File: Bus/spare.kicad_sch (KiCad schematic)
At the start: 2 parts, among them J16 Conn_01x06_Pin, J17 Conn_01x03_Pin

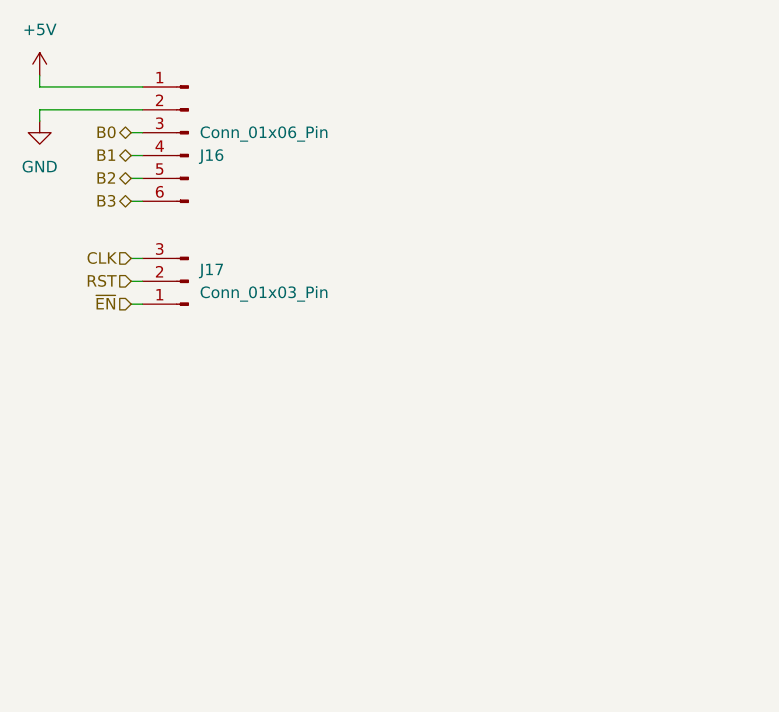
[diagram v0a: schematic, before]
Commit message: Updated bus schematic control pins and added spare bus connection
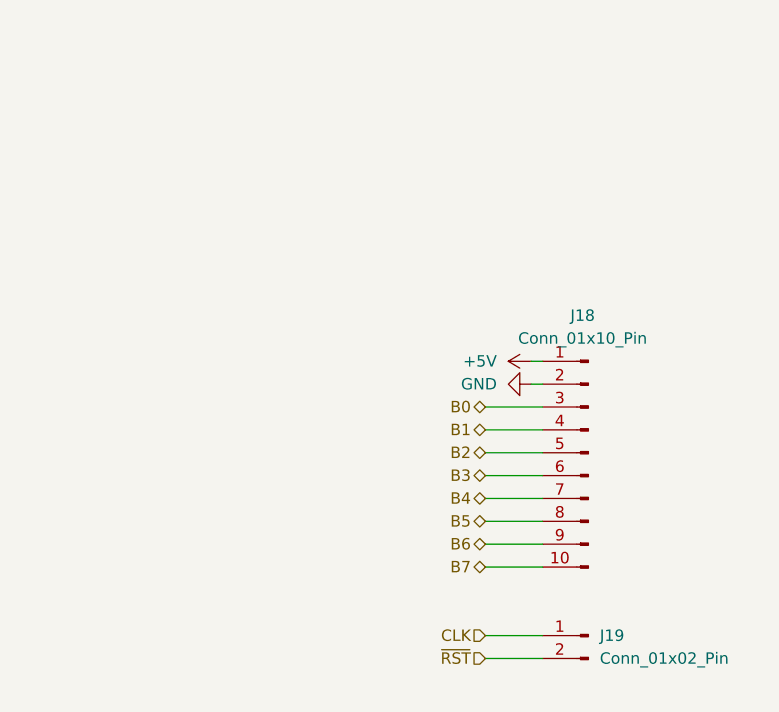
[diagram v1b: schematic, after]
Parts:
- removed J16: Conn_01x06_Pin, Connector_PinHeader_2.54mm:PinHeader_1x06_P2.54mm_Vertical, symbol Connector:Conn_01x06_Pin
- removed J17: Conn_01x03_Pin, Connector_PinHeader_2.54mm:PinHeader_1x03_P2.54mm_Vertical, symbol Connector:Conn_01x03_Pin
- added J18: Conn_01x10_Pin, Connector_PinHeader_2.54mm:PinHeader_1x10_P2.54mm_Vertical, symbol Connector:Conn_01x10_Pin
- added J19: Conn_01x02_Pin, symbol Connector:Conn_01x02_Pin
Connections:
- net +5V: now also J18.1 (Pin_1)
- net B0: now also J18.3 (Pin_3)
- net B1: now also J18.4 (Pin_4)
- net B2: now also J18.5 (Pin_5)
- net B3: now also J18.6 (Pin_6)
- net CLK: now also J19.1 (Pin_1)
- net GND: now also J18.2 (Pin_2)
- new net B4: J18.7 (Pin_7)
- new net B5: J18.8 (Pin_8)
- new net B6: J18.9 (Pin_9)
- new net B7: J18.10 (Pin_10)
- new net ~{RST}: J19.2 (Pin_2)

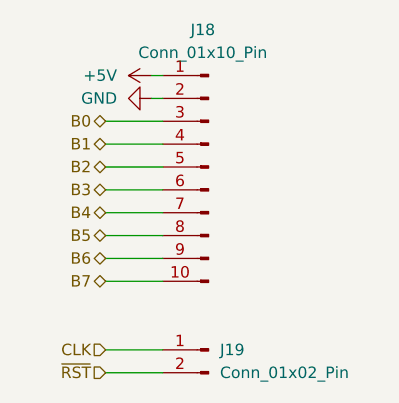
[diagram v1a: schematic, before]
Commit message: Updated bus schmatic pins to match final layouts
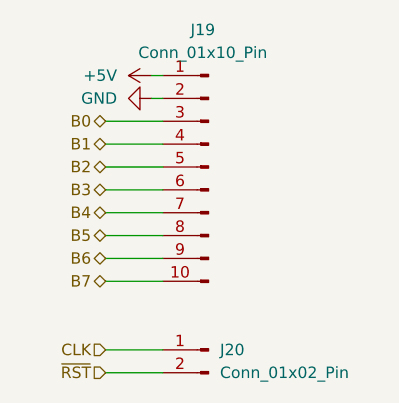
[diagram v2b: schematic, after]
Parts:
- renumbered J18 to J19, J19 to J20
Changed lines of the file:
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@@
 		(on_board yes)
 		(dnp no)
-		(property "Reference" "J18"
+		(property "Reference" "J19"
 			(at 149.225 85.09 0)
 			(effects
@@
 			(project "bus"
 				(path "/37ae8b13-e183-404e-b70a-681e1af60f55/662d6a90-2c83-4a1e-be16-f45c39c56db0"
-					(reference "J18")
+					(reference "J19")
 					(unit 1)
 				)
@@
 		(dnp no)
 		(fields_autoplaced yes)
-		(property "Reference" "#PWR023"
+		(property "Reference" "#PWR022"
 			(at 137.16 92.71 0)
 			(effects
@@
 			(project "bus"
 				(path "/37ae8b13-e183-404e-b70a-681e1af60f55/662d6a90-2c83-4a1e-be16-f45c39c56db0"
-					(reference "#PWR023")
+					(reference "#PWR022")
 					(unit 1)
 				)
@@
 		(dnp no)
 		(fields_autoplaced yes)
-		(property "Reference" "#PWR022"
+		(property "Reference" "#PWR021"
 			(at 147.32 90.17 0)
 			(effects
@@
 			(project "bus"
 				(path "/37ae8b13-e183-404e-b70a-681e1af60f55/662d6a90-2c83-4a1e-be16-f45c39c56db0"
-					(reference "#PWR022")
+					(reference "#PWR021")
 					(unit 1)
 				)
@@
 		(dnp no)
 		(fields_autoplaced yes)
-		(property "Reference" "J19"
+		(property "Reference" "J20"
 			(at 151.13 120.6499 0)
 			(effects
@@
 			(project ""
 				(path "/37ae8b13-e183-404e-b70a-681e1af60f55/662d6a90-2c83-4a1e-be16-f45c39c56db0"
-					(reference "J19")
-					(unit 1)
-				)
+					(reference "J20")
+					(unit 1)
+				)

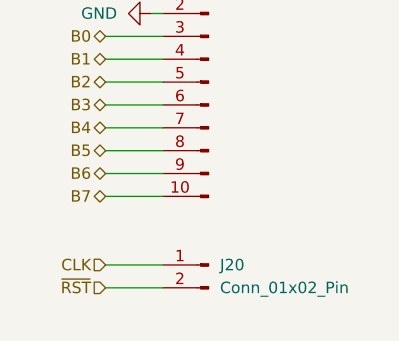
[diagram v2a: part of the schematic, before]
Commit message: Added ~clk to the spare signals
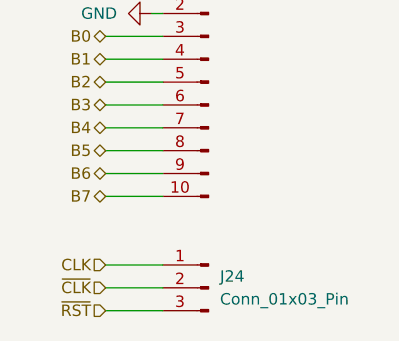
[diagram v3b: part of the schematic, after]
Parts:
- removed J20: Conn_01x02_Pin, symbol Connector:Conn_01x02_Pin
- added J24: Conn_01x03_Pin, symbol Connector:Conn_01x03_Pin
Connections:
- net CLK: now also J24.1 (Pin_1)
- net ~{RST}: now also J24.3 (Pin_3)
- new net ~{CLK}: J24.2 (Pin_2)
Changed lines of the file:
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@@
+	(wire
+		(pts
+			(xy 138.43 125.73) (xy 144.78 125.73)
+		)
+		(stroke
+			(width 0)
+			(type default)
+		)
+	)
+	(wire
+		(pts
+			(xy 144.78 105.41) (xy 138.43 105.41)
+		)
+		(stroke
+			(width 0)
+			(type default)
+		)
+	)
+	(wire
+		(pts
+			(xy 144.78 110.49) (xy 138.43 110.49)
+		)
+		(stroke
+			(width 0)
+			(type default)
+		)
+	)
+	(wire
+		(pts
+			(xy 144.78 107.95) (xy 138.43 107.95)
+		)
+		(stroke
+			(width 0)
+			(type default)
+		)
+	)
 	(wire
 		(pts
 			(xy 138.43 123.19) (xy 144.78 123.19)
-		)
-		(stroke
-			(width 0)
-			(type default)
-		)
-	)
-	(wire
-		(pts
-			(xy 144.78 105.41) (xy 138.43 105.41)
-		)
-		(stroke
-			(width 0)
-			(type default)
-		)
-	)
-	(wire
-		(pts
-			(xy 144.78 110.49) (xy 138.43 110.49)
-		)
-		(stroke
-			(width 0)
-			(type default)
-		)
-	)
-	(wire
-		(pts
-			(xy 144.78 107.95) (xy 138.43 107.95)
 		)
 		(stroke
@@
 	(hierarchical_label "~{RST}"
 		(shape input)
-		(at 138.43 123.19 180)
+		(at 138.43 125.73 180)
 		(fields_autoplaced yes)
 		(effects
@@
 		(shape input)
 		(at 138.43 120.65 180)
+		(fields_autoplaced yes)
+		(effects
+			(font
+				(size 1.27 1.27)
+			)
+			(justify right)
+		)
+	)
+	(hierarchical_label "~{CLK}"
+		(shape input)
+		(at 138.43 123.19 180)
 		(fields_autoplaced yes)
 		(effects
@@
 	)
 	(symbol
-		(lib_id "Connector:Conn_01x02_Pin")
-		(at 149.86 120.65 0)
+		(lib_id "Connector:Conn_01x03_Pin")
+		(at 149.86 123.19 0)
 		(mirror y)
 		(unit 1)
@@
 		(dnp no)
 		(fields_autoplaced yes)
-		(property "Reference" "J20"
-			(at 151.13 120.6499 0)
+		(property "Reference" "J24"
+			(at 151.13 121.9199 0)
 			(effects
 				(font
@@
 			)
 		)
-		(property "Value" "Conn_01x02_Pin"
-			(at 151.13 123.1899 0)
+		(property "Value" "Conn_01x03_Pin"
+			(at 151.13 124.4599 0)
 			(effects
 				(font
@@
 		)
 		(property "Footprint" ""
-			(at 149.86 120.65 0)
+			(at 149.86 123.19 0)
 			(effects
 				(font
@@
 		)
 		(property "Datasheet" "~"
-			(at 149.86 120.65 0)
-			(effects
-				(font
-					(size 1.27 1.27)
-				)
-				(hide yes)
-			)
-		)
-		(property "Description" "Generic connector, single row, 01x02, script generated"
-			(at 149.86 120.65 0)
-			(effects
-				(font
-					(size 1.27 1.27)
-				)
-				(hide yes)
-			)
+			(at 149.86 123.19 0)
+			(effects
+				(font
+					(size 1.27 1.27)
+				)
+				(hide yes)
+			)
+		)
+		(property "Description" "Generic connector, single row, 01x03, script generated"
+			(at 149.86 123.19 0)
+			(effects
+				(font
+					(size 1.27 1.27)
+				)
+				(hide yes)
+			)
+		)
+		(pin "3"
+		)
+		(pin "2"
 		)
 		(pin "1"
-		)
-		(pin "2"
 		)
 		(instances
 			(project ""
 				(path "/37ae8b13-e183-404e-b70a-681e1af60f55/662d6a90-2c83-4a1e-be16-f45c39c56db0"
-					(reference "J20")
+					(reference "J24")
 					(unit 1)
 				)

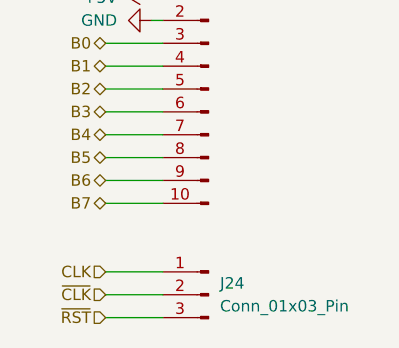
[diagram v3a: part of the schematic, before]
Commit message: Fixed mismatched RAM labels
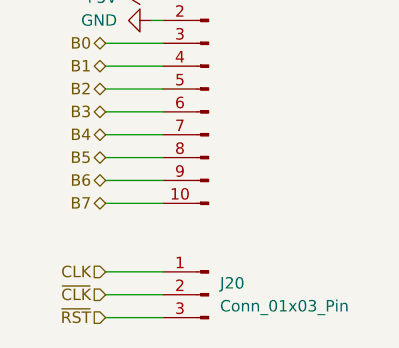
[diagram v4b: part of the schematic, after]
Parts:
- renumbered J24 to J20
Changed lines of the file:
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@@
 		(dnp no)
 		(fields_autoplaced yes)
-		(property "Reference" "J24"
+		(property "Reference" "J20"
 			(at 151.13 121.9199 0)
 			(effects
@@
 			(project ""
 				(path "/37ae8b13-e183-404e-b70a-681e1af60f55/662d6a90-2c83-4a1e-be16-f45c39c56db0"
-					(reference "J24")
+					(reference "J20")
 					(unit 1)
 				)

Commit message: Added pins to bus PCB. Oh boy it's going to be long
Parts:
- J20: footprint (none) -> Connector_PinHeader_2.54mm:PinHeader_1x03_P2.54mm_Vertical
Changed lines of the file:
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@@
 			)
 		)
-		(property "Footprint" ""
+		(property "Footprint" "Connector_PinHeader_2.54mm:PinHeader_1x03_P2.54mm_Vertical"
 			(at 149.86 123.19 0)
 			(effects
